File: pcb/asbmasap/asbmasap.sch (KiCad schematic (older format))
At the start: 53 parts, among them J1 USB_C_Receptacle_USB2.0, Q1 Q_PMOS_DGS, SW1 SW_Push, U1 MCP73831-2-OT, U2 TPS61200DRC, U3 nRF52840, Y1 32.768kHz, Y2 32MHz

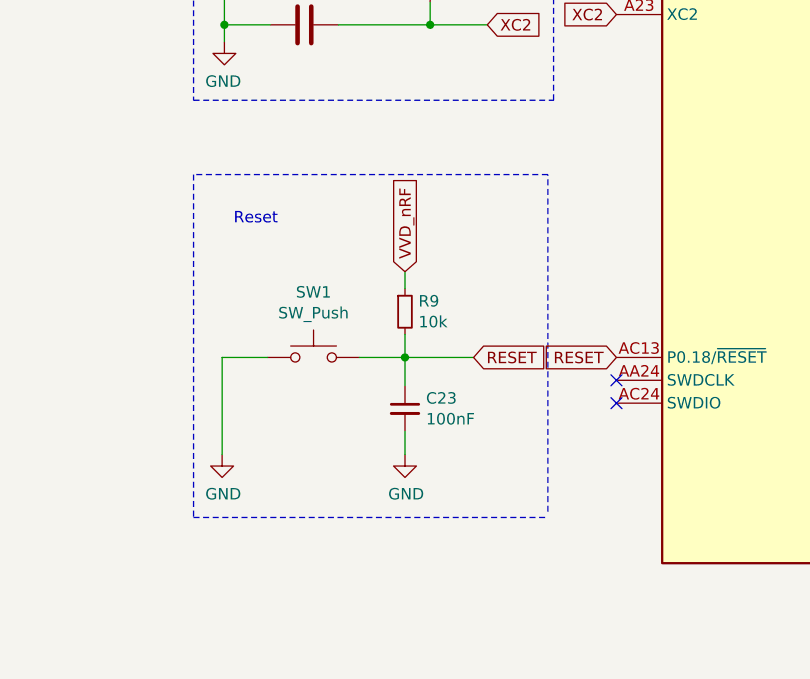
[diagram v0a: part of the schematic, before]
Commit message: feat(pcb): simplify reset circuit
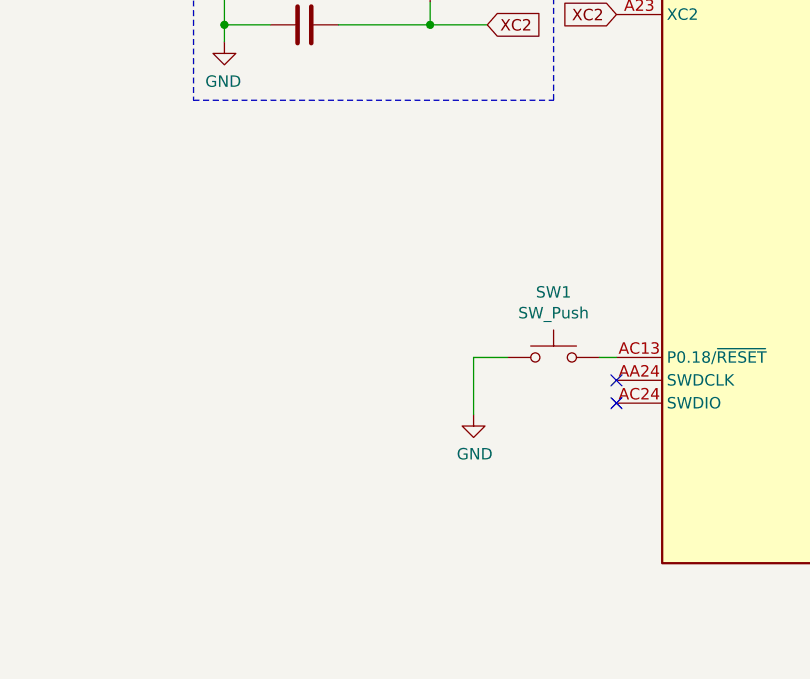
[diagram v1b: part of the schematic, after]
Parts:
- removed C23: 100nF, symbol Device:C_Small
- removed R9: 10k, symbol Device:R_Small
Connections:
- net RESET: no longer names the net of SW1.2, U3.AC13 (P0.18/~RESET)
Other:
- note removed: "Reset"
- moved on the sheet: SW1
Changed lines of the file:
@@
 Comment4 ""
 $EndDescr
-$Comp
-L Connector:USB_C_Receptacle_USB2.0 J1
-U 1 1 61169404
-P 1650 2275
-F 0 "J1" H 1757 3142 50  0000 C CNN
-F 1 "USB_C_Receptacle_USB2.0" H 1757 3051 50  0000 C CNN
-F 2 "" H 1800 2275 50  0001 C CNN
-F 3 "https://www.usb.org/sites/default/files/documents/usb_type-c.zip" H 1800 2275 50  0001 C CNN
-	1    1650 2275
-	1    0    0    -1
-$EndComp
 NoConn ~ 1350 3175
 NoConn ~ 2250 2775
@@
 Wire Notes Line
 	7950 6275 10350 6275
-Text GLabel 10625 10250 0    50   Input ~ 0
-RESET
-Text GLabel 10000 10250 2    50   Input ~ 0
-RESET
-Text GLabel 9700 9875 1    50   Input ~ 0
-VVD_nRF
-$Comp
-L Device:R_Small R9
-U 1 1 61716A2B
-P 9700 10050
-F 0 "R9" H 9759 10096 50  0000 L CNN
-F 1 "10k" H 9759 10005 50  0000 L CNN
-F 2 "" H 9700 10050 50  0001 C CNN
-F 3 "~" H 9700 10050 50  0001 C CNN
-	1    9700 10050
-	1    0    0    -1
-$EndComp
-$Comp
-L Device:C_Small C23
-U 1 1 6171E4F3
-P 9700 10475
-F 0 "C23" H 9792 10521 50  0000 L CNN
-F 1 "100nF" H 9792 10430 50  0000 L CNN
-F 2 "" H 9700 10475 50  0001 C CNN
-F 3 "~" H 9700 10475 50  0001 C CNN
-	1    9700 10475
-	1    0    0    -1
-$EndComp
 $Comp
 L Switch:SW_Push SW1
 U 1 1 6171F16D
-P 9300 10250
-F 0 "SW1" H 9300 10535 50  0000 C CNN
-F 1 "SW_Push" H 9300 10444 50  0000 C CNN
-F 2 "" H 9300 10450 50  0001 C CNN
-F 3 "~" H 9300 10450 50  0001 C CNN
-	1    9300 10250
-	1    0    0    -1
-$EndComp
-Wire Wire Line
-	10000 10250 9700 10250
-Wire Wire Line
-	9700 10150 9700 10250
-Connection ~ 9700 10250
-Wire Wire Line
-	9700 10250 9500 10250
-Wire Wire Line
-	9700 10250 9700 10375
-Wire Wire Line
-	9700 9875 9700 9950
-Wire Wire Line
-	9100 10250 8900 10250
-Wire Wire Line
-	8900 10250 8900 10675
-Wire Wire Line
-	9700 10575 9700 10675
-$Comp
-L power:GND #PWR0116
-U 1 1 617481A9
-P 9700 10675
-F 0 "#PWR0116" H 9700 10425 50  0001 C CNN
-F 1 "GND" H 9705 10502 50  0000 C CNN
-F 2 "" H 9700 10675 50  0001 C CNN
-F 3 "" H 9700 10675 50  0001 C CNN
-	1    9700 10675
-	1    0    0    -1
-$EndComp
+P 10350 10250
+F 0 "SW1" H 10350 10535 50  0000 C CNN
+F 1 "SW_Push" H 10350 10444 50  0000 C CNN
+F 2 "" H 10350 10450 50  0001 C CNN
+F 3 "~" H 10350 10450 50  0001 C CNN
+	1    10350 10250
+	1    0    0    -1
+$EndComp
+Wire Wire Line
+	10150 10250 10000 10250
+Wire Wire Line
+	10000 10250 10000 10500
 $Comp
 L power:GND #PWR0117
 U 1 1 61748C55
-P 8900 10675
-F 0 "#PWR0117" H 8900 10425 50  0001 C CNN
-F 1 "GND" H 8905 10502 50  0000 C CNN
-F 2 "" H 8900 10675 50  0001 C CNN
-F 3 "" H 8900 10675 50  0001 C CNN
-	1    8900 10675
-	1    0    0    -1
-$EndComp
-Text Notes 8950 9675 0    50   ~ 0
-Reset
-Wire Notes Line
-	10325 10925 10325 9450
-Wire Notes Line
-	10325 9450 8775 9450
-Wire Notes Line
-	8775 9450 8775 10950
-Wire Notes Line
-	8775 10950 10325 10950
+P 10000 10500
+F 0 "#PWR0117" H 10000 10250 50  0001 C CNN
+F 1 "GND" H 10005 10327 50  0000 C CNN
+F 2 "" H 10000 10500 50  0001 C CNN
+F 3 "" H 10000 10500 50  0001 C CNN
+	1    10000 10500
+	1    0    0    -1
+$EndComp
 Wire Wire Line
 	8500 3425 8500 3075
@@
 NoConn ~ 10625 10350
 NoConn ~ 10625 10450
+$Comp
+L Connector:USB_C_Receptacle_USB2.0 J1
+U 1 1 61169404
+P 1650 2275
+F 0 "J1" H 1757 3142 50  0000 C CNN
+F 1 "USB_C_Receptacle_USB2.0" H 1757 3051 50  0000 C CNN
+F 2 "" H 1800 2275 50  0001 C CNN
+F 3 "https://www.usb.org/sites/default/files/documents/usb_type-c.zip" H 1800 2275 50  0001 C CNN
+	1    1650 2275
+	1    0    0    -1
+$EndComp
+Wire Wire Line
+	10550 10250 10625 10250
 $EndSCHEMATC

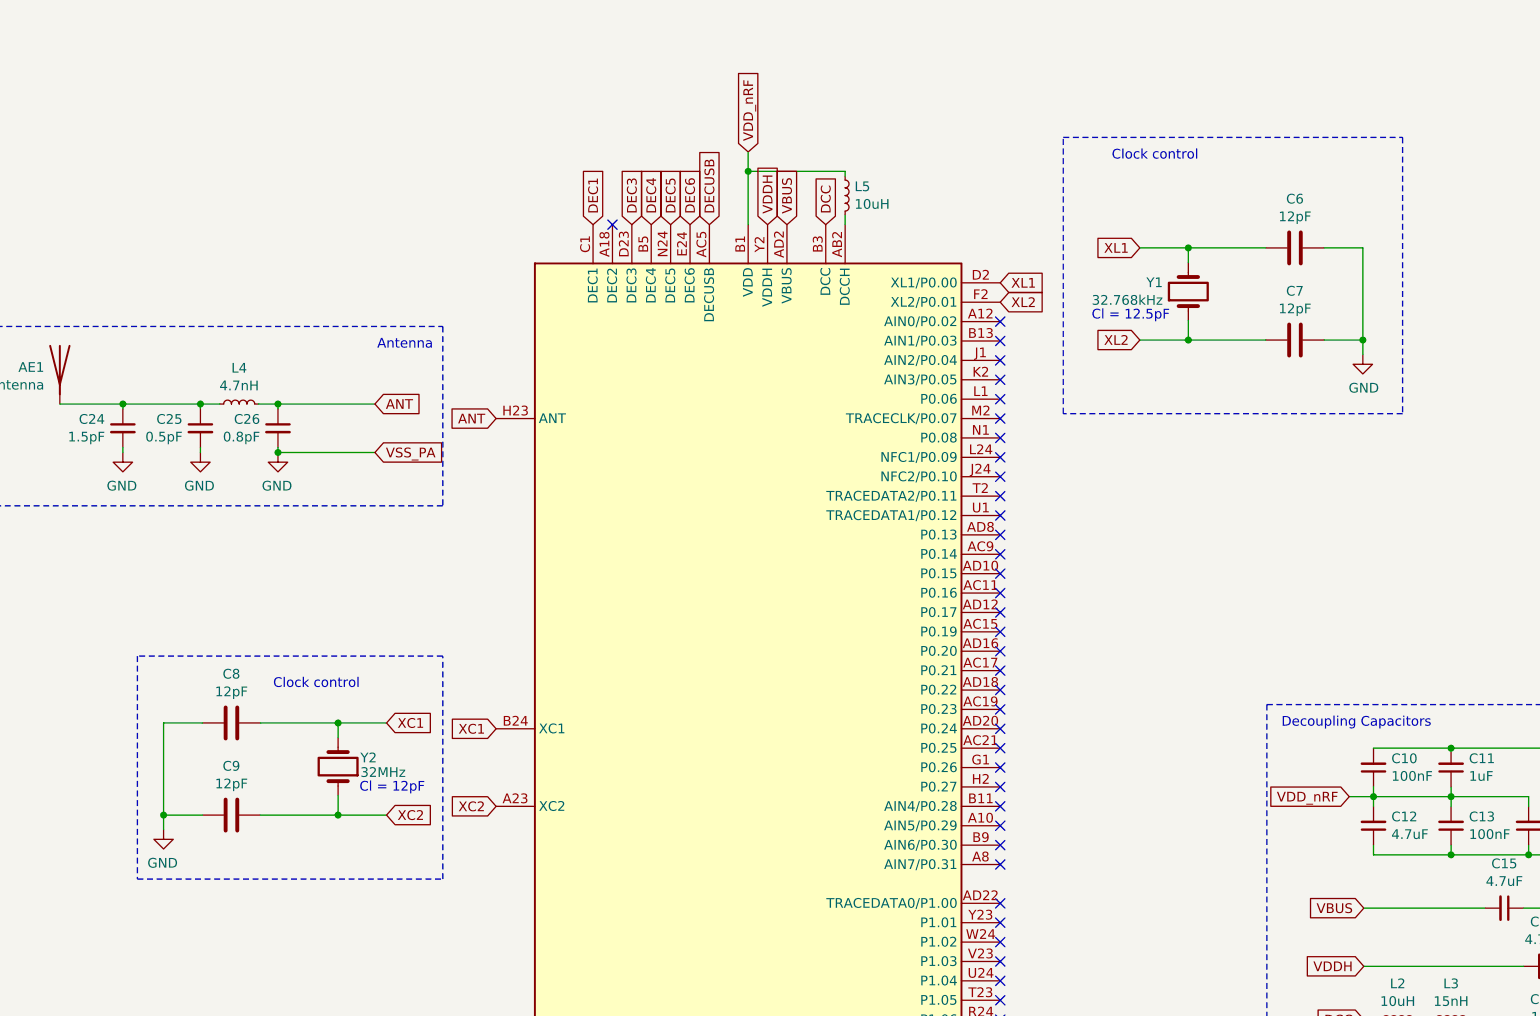
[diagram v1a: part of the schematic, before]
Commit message: refactor(pcb): simplify clock control on schema
Update asbmasap.sch
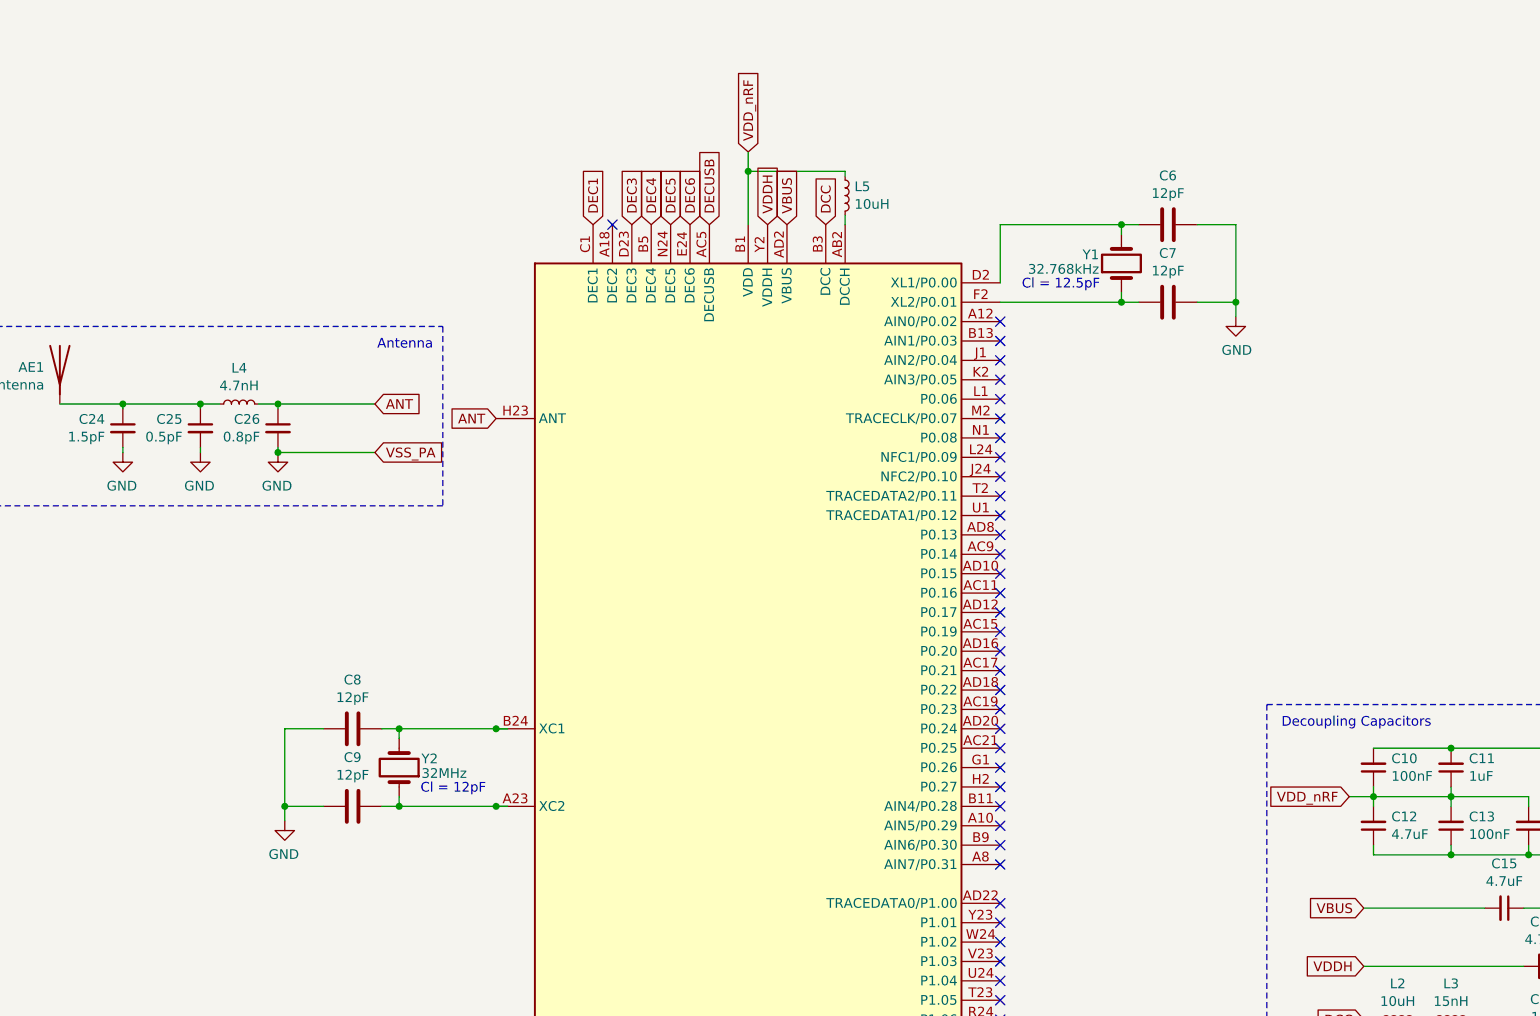
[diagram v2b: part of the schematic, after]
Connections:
- net labels removed: XC1, XC2, XL1, XL2
- wire segments 192 -> 195
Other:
- note removed: "Clock control"
- moved on the sheet: C8, C9, Y2
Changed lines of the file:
@@
 Wire Wire Line
 	9125 3525 9600 3525
-$Comp
-L MCU_Nordic:nRF52840 U3
-U 1 1 61223031
-P 11925 8550
-F 0 "U3" H 11925 5661 50  0000 C CNN
-F 1 "nRF52840" H 11925 5570 50  0000 C CNN
-F 2 "Package_DFN_QFN:Nordic_AQFN-73-1EP_7x7mm_P0.5mm" H 11925 5650 50  0001 C CNN
-F 3 "http://infocenter.nordicsemi.com/topic/com.nordic.infocenter.nrf52/dita/nrf52/chips/nrf52840.html" H 11275 10450 50  0001 C CNN
-	1    11925 8550
-	1    0    0    -1
-$EndComp
 Wire Wire Line
 	13225 10950 13325 10950
@@
 Text GLabel 13325 11050 2    50   BiDi ~ 0
 USB_D+
-Text Notes 13800 5425 0    50   ~ 0
-Clock control
-Text GLabel 10625 8350 0    50   Input ~ 0
-XC1
-Text GLabel 10625 8750 0    50   Input ~ 0
-XC2
-Text GLabel 13225 6050 2    50   Input ~ 0
-XL1
-Text GLabel 13225 6150 2    50   Input ~ 0
-XL2
 $Comp
 L Device:C_Small C22
@@
 Wire Wire Line
 	8500 3425 8500 3075
-Connection ~ 9810 8795
-Wire Wire Line
-	10060 8795 9810 8795
-Wire Wire Line
-	9810 8320 9410 8320
-Wire Wire Line
-	9810 8320 9810 8395
-Connection ~ 9810 8320
-Wire Wire Line
-	10060 8320 9810 8320
-Wire Wire Line
-	9810 8795 9810 8695
-Wire Wire Line
-	9410 8795 9810 8795
-Wire Wire Line
-	8910 8795 8910 8870
-Connection ~ 8910 8795
-Wire Wire Line
-	9110 8795 8910 8795
-Wire Wire Line
-	8910 8320 8910 8795
-Wire Wire Line
-	9110 8320 8910 8320
-$Comp
-L power:GND #PWR0109
-U 1 1 61250AE5
-P 8910 8870
-F 0 "#PWR0109" H 8910 8620 50  0001 C CNN
-F 1 "GND" H 8915 8697 50  0000 C CNN
-F 2 "" H 8910 8870 50  0001 C CNN
-F 3 "" H 8910 8870 50  0001 C CNN
-	1    8910 8870
-	-1   0    0    -1
-$EndComp
-$Comp
-L Device:C C9
-U 1 1 6124DCA3
-P 9260 8795
-F 0 "C9" V 9008 8795 50  0000 C CNN
-F 1 "12pF" V 9099 8795 50  0000 C CNN
-F 2 "" H 9298 8645 50  0001 C CNN
-F 3 "~" H 9260 8795 50  0001 C CNN
-	1    9260 8795
-	0    -1   1    0
-$EndComp
-$Comp
-L Device:C C8
-U 1 1 6124D361
-P 9260 8320
-F 0 "C8" V 9008 8320 50  0000 C CNN
-F 1 "12pF" V 9099 8320 50  0000 C CNN
-F 2 "" H 9298 8170 50  0001 C CNN
-F 3 "~" H 9260 8320 50  0001 C CNN
-	1    9260 8320
-	0    -1   1    0
-$EndComp
-$Comp
-L Device:Crystal Y2
-U 1 1 6124BD5F
-P 9810 8545
-F 0 "Y2" V 9855 8660 50  0000 L CNN
-F 1 "32MHz" V 9780 8660 50  0000 L CNN
-F 2 "" H 9810 8545 50  0001 C CNN
-F 3 "~" H 9810 8545 50  0001 C CNN
-	1    9810 8545
-	0    1    -1   0
-$EndComp
-Text GLabel 10060 8795 2    50   Input ~ 0
-XC2
-Text GLabel 10060 8320 2    50   Input ~ 0
-XC1
-Connection ~ 14195 6345
-Wire Wire Line
-	13945 6345 14195 6345
-Wire Wire Line
-	14195 5870 14595 5870
-Wire Wire Line
-	14195 5870 14195 5945
-Connection ~ 14195 5870
-Wire Wire Line
-	13945 5870 14195 5870
-Wire Wire Line
-	14195 6345 14195 6245
-Wire Wire Line
-	14595 6345 14195 6345
-Wire Wire Line
-	14895 6345 15095 6345
-Wire Wire Line
-	14895 5870 15095 5870
-$Comp
-L power:GND #PWR0110
-U 1 1 6126F786
-P 15095 6420
-F 0 "#PWR0110" H 15095 6170 50  0001 C CNN
-F 1 "GND" H 15100 6247 50  0000 C CNN
-F 2 "" H 15095 6420 50  0001 C CNN
-F 3 "" H 15095 6420 50  0001 C CNN
-	1    15095 6420
-	1    0    0    -1
-$EndComp
-$Comp
-L Device:C C7
-U 1 1 6126F77C
-P 14745 6345
-F 0 "C7" V 14493 6345 50  0000 C CNN
-F 1 "12pF" V 14584 6345 50  0000 C CNN
-F 2 "" H 14783 6195 50  0001 C CNN
-F 3 "~" H 14745 6345 50  0001 C CNN
-	1    14745 6345
-	0    1    1    0
-$EndComp
-$Comp
-L Device:C C6
-U 1 1 6126F772
-P 14745 5870
-F 0 "C6" V 14493 5870 50  0000 C CNN
-F 1 "12pF" V 14584 5870 50  0000 C CNN
-F 2 "" H 14783 5720 50  0001 C CNN
-F 3 "~" H 14745 5870 50  0001 C CNN
-	1    14745 5870
-	0    1    1    0
-$EndComp
-$Comp
-L Device:Crystal Y1
-U 1 1 6126F768
-P 14195 6095
-F 0 "Y1" V 14241 6226 50  0000 L CNN
-F 1 "32.768kHz" V 14150 6226 50  0000 L CNN
-F 2 "" H 14195 6095 50  0001 C CNN
-F 3 "~" H 14195 6095 50  0001 C CNN
-	1    14195 6095
-	0    -1   -1   0
-$EndComp
-Text GLabel 13945 6345 0    50   Input ~ 0
-XL2
-Text GLabel 13945 5870 0    50   Input ~ 0
-XL1
-Wire Wire Line
-	15095 5870 15095 6345
-Connection ~ 15095 6345
-Wire Wire Line
-	15095 6345 15095 6420
-Text Notes 9920 8685 0    50   ~ 0
-Cl = 12pF
-Text Notes 14100 6250 2    50   ~ 0
-Cl = 12.5pF
 Wire Wire Line
 	12425 5700 12425 5750
@@
 Text GLabel 12025 11350 3    50   Input ~ 0
 VSS_PA
-Wire Notes Line
-	15300 5300 15300 6725
-Wire Notes Line
-	15300 6725 13550 6725
-Wire Notes Line
-	13550 6725 13550 5300
-Wire Notes Line
-	13550 5300 15300 5300
-Wire Notes Line
-	8775 9125 10350 9125
-Wire Notes Line
-	10350 9125 10350 7975
-Wire Notes Line
-	10350 7975 8775 7975
-Wire Notes Line
-	8775 7975 8775 9125
-Text Notes 9475 8150 0    50   ~ 0
-Clock control
 Text GLabel 10625 6750 0    50   Input ~ 0
 ANT
@@
 Wire Wire Line
 	10550 10250 10625 10250
+$Comp
+L MCU_Nordic:nRF52840 U3
+U 1 1 61223031
+P 11925 8550
+F 0 "U3" H 11925 5661 50  0000 C CNN
+F 1 "nRF52840" H 11925 5570 50  0000 C CNN
+F 2 "Package_DFN_QFN:Nordic_AQFN-73-1EP_7x7mm_P0.5mm" H 11925 5650 50  0001 C CNN
+F 3 "http://infocenter.nordicsemi.com/topic/com.nordic.infocenter.nrf52/dita/nrf52/chips/nrf52840.html" H 11275 10450 50  0001 C CNN
+	1    11925 8550
+	1    0    0    -1
+$EndComp
+Wire Wire Line
+	9535 8750 9535 8825
+Wire Wire Line
+	10125 8750 10625 8750
+Wire Wire Line
+	10125 8700 10125 8750
+Wire Wire Line
+	10125 8350 10625 8350
+Wire Wire Line
+	10125 8400 10125 8350
+Wire Wire Line
+	9735 8750 9535 8750
+Wire Wire Line
+	9735 8350 9535 8350
+$Comp
+L power:GND #PWR0109
+U 1 1 61250AE5
+P 9535 8825
+F 0 "#PWR0109" H 9535 8575 50  0001 C CNN
+F 1 "GND" H 9540 8652 50  0000 C CNN
+F 2 "" H 9535 8825 50  0001 C CNN
+F 3 "" H 9535 8825 50  0001 C CNN
+	1    9535 8825
+	-1   0    0    -1
+$EndComp
+$Comp
+L Device:C C9
+U 1 1 6124DCA3
+P 9885 8750
+F 0 "C9" V 9633 8750 50  0000 C CNN
+F 1 "12pF" V 9724 8750 50  0000 C CNN
+F 2 "" H 9923 8600 50  0001 C CNN
+F 3 "~" H 9885 8750 50  0001 C CNN
+	1    9885 8750
+	0    -1   1    0
+$EndComp
+$Comp
+L Device:C C8
+U 1 1 6124D361
+P 9885 8350
+F 0 "C8" V 9633 8350 50  0000 C CNN
+F 1 "12pF" V 9724 8350 50  0000 C CNN
+F 2 "" H 9923 8200 50  0001 C CNN
+F 3 "~" H 9885 8350 50  0001 C CNN
+	1    9885 8350
+	0    -1   1    0
+$EndComp
+Text Notes 10235 8690 0    50   ~ 0
+Cl = 12pF
+$Comp
+L Device:Crystal Y2
+U 1 1 6124BD5F
+P 10125 8550
+F 0 "Y2" V 10170 8665 50  0000 L CNN
+F 1 "32MHz" V 10095 8665 50  0000 L CNN
+F 2 "" H 10125 8550 50  0001 C CNN
+F 3 "~" H 10125 8550 50  0001 C CNN
+	1    10125 8550
+	0    1    -1   0
+$EndComp
+Connection ~ 10125 8350
+Wire Wire Line
+	10035 8350 10125 8350
+Connection ~ 10125 8750
+Wire Wire Line
+	10035 8750 10125 8750
+Connection ~ 9535 8750
+Wire Wire Line
+	9535 8350 9535 8750
+Connection ~ 10625 8750
+Wire Wire Line
+	10625 8750 10685 8750
+Connection ~ 10625 8350
+Wire Wire Line
+	10625 8350 10685 8350
+Wire Wire Line
+	14440 5750 14440 6150
+Wire Wire Line
+	13940 6150 13850 6150
+Wire Wire Line
+	13940 5750 13850 5750
+$Comp
+L Device:Crystal Y1
+U 1 1 6197F8CB
+P 13850 5950
+F 0 "Y1" V 13895 6065 50  0000 L CNN
+F 1 "32.768kHz" V 13820 6065 50  0000 L CNN
+F 2 "" H 13850 5950 50  0001 C CNN
+F 3 "~" H 13850 5950 50  0001 C CNN
+	1    13850 5950
+	0    -1   -1   0
+$EndComp
+Text Notes 13740 6090 2    50   ~ 0
+Cl = 12.5pF
+$Comp
+L power:GND #PWR0110
+U 1 1 6197F8DE
+P 14440 6225
+F 0 "#PWR0110" H 14440 5975 50  0001 C CNN
+F 1 "GND" H 14445 6052 50  0000 C CNN
+F 2 "" H 14440 6225 50  0001 C CNN
+F 3 "" H 14440 6225 50  0001 C CNN
+	1    14440 6225
+	1    0    0    -1
+$EndComp
+Wire Wire Line
+	14240 5750 14440 5750
+Wire Wire Line
+	14240 6150 14440 6150
+Wire Wire Line
+	13850 5800 13850 5750
+Connection ~ 13850 5750
+Wire Wire Line
+	13850 6100 13850 6150
+Connection ~ 13850 6150
+Connection ~ 14440 6150
+Wire Wire Line
+	14440 6150 14440 6225
+$Comp
+L Device:C C7
+U 1 1 6197F8D8
+P 14090 6150
+F 0 "C7" V 13838 6150 50  0000 C CNN
+F 1 "12pF" V 13929 6150 50  0000 C CNN
+F 2 "" H 14128 6000 50  0001 C CNN
+F 3 "~" H 14090 6150 50  0001 C CNN
+	1    14090 6150
+	0    1    1    0
+$EndComp
+$Comp
+L Device:C C6
+U 1 1 6197F8D2
+P 14090 5750
+F 0 "C6" V 13838 5750 50  0000 C CNN
+F 1 "12pF" V 13929 5750 50  0000 C CNN
+F 2 "" H 14128 5600 50  0001 C CNN
+F 3 "~" H 14090 5750 50  0001 C CNN
+	1    14090 5750
+	0    1    1    0
+$EndComp
+Wire Wire Line
+	13225 6150 13850 6150
+Wire Wire Line
+	13225 6050 13225 5750
+Wire Wire Line
+	13225 5750 13850 5750
 $EndSCHEMATC

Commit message: feat(pcb): add VBUS output
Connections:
- wire segments 195 -> 196
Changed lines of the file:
@@
 Wire Wire Line
 	13225 5750 13850 5750
+Text GLabel 3650 1200 1    50   Output ~ 0
+VBUS
+Wire Wire Line
+	3650 1350 3650 1200
+Connection ~ 3650 1350
 $EndSCHEMATC
